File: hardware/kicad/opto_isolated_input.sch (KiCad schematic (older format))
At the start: 9 parts, among them Q1 BC547, Q2 BC337, U6 SFH617A-1, U7 MAX6816

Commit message: Stuff
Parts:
- Q2: value BC337 -> BC337-40
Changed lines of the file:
@@
 AR Path="/62FB890E/62EA87F7" Ref="Q14"  Part="1"
 F 0 "Q2" H 5791 3746 50  0000 L CNN
-F 1 "BC337" H 5791 3655 50  0000 L CNN
+F 1 "BC337-40" H 5791 3655 50  0000 L CNN
 F 2 "Package_TO_SOT_THT:TO-92_Inline" H 5800 3625 50  0001 L CIN
 F 3 "https://diotec.com/tl_files/diotec/files/pdf/datasheets/bc337.pdf" H 5600 3700 50  0001 L CNN
@@
 Text HLabel 7600 3500 2    50   Output ~ 0
 OII_OUT
-Text HLabel 7600 4200 2    50   UnSpc ~ 0
+Text HLabel 7650 4200 2    50   UnSpc ~ 0
 OII_OUT_GND
 $Comp

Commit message: Terak
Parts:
- D10: value IN4148 -> IN4007
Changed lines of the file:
@@
 AR Path="/62FB890E/62FE9B9E" Ref="D16"  Part="1"
 F 0 "D10" H 4750 3250 50  0000 L CNN
-F 1 "IN4148" H 5000 3250 50  0000 L CNN
+F 1 "IN4007" H 5000 3250 50  0000 L CNN
 F 2 "Diode_THT:D_A-405_P2.54mm_Vertical_AnodeUp" H 4950 3300 50  0001 C CNN
 F 3 "~" H 4950 3300 50  0001 C CNN

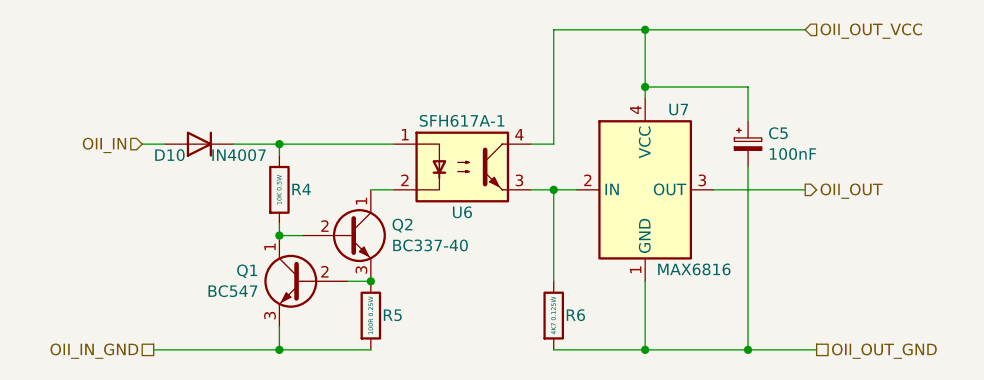
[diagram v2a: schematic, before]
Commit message: Add mount holes
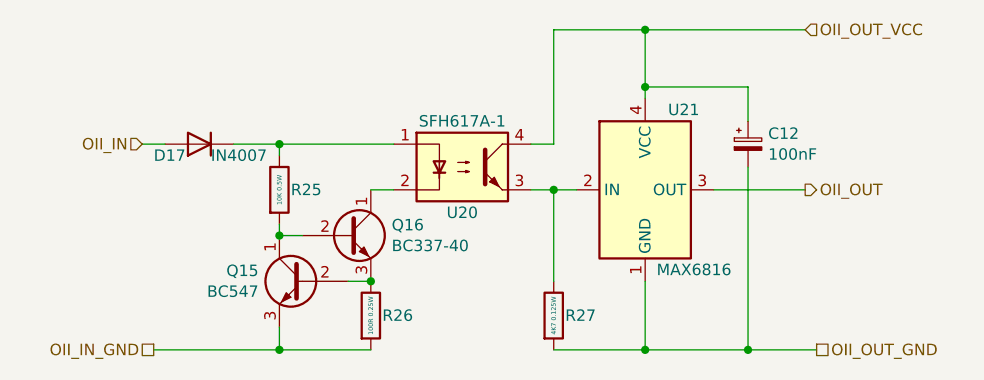
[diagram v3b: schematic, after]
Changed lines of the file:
@@
 AR Path="/62F45EE0/62EBA913" Ref="U16"  Part="1"
 AR Path="/62FB890E/62EBA913" Ref="U18"  Part="1"
-F 0 "U6" H 6100 3200 50  0000 C CNN
+F 0 "U20" H 6100 3200 50  0000 C CNN
 F 1 "SFH617A-1" H 6100 3600 50  0000 C CNN
 F 2 "Package_DIP:DIP-4_W7.62mm" H 5900 3200 50  0001 L CIN
@@
 AR Path="/62F45EE0/62ED7963" Ref="R19"  Part="1"
 AR Path="/62FB890E/62ED7963" Ref="R22"  Part="1"
-F 0 "R4" H 5350 3500 50  0000 L CNN
+F 0 "R25" H 5350 3500 50  0000 L CNN
 F 1 "10K 0.5W" V 5300 3500 20  0000 C CNN
 F 2 "Resistor_THT:R_Axial_DIN0207_L6.3mm_D2.5mm_P2.54mm_Vertical" V 5230 3500 50  0001 C CNN
@@
 AR Path="/62F45EE0/62F493CD" Ref="R20"  Part="1"
 AR Path="/62FB890E/62F493CD" Ref="R23"  Part="1"
-F 0 "R5" H 5750 4050 50  0000 L CNN
+F 0 "R26" H 5750 4050 50  0000 L CNN
 F 1 "100R 0.25W" V 5700 4050 20  0000 C CNN
 F 2 "Resistor_THT:R_Axial_DIN0207_L6.3mm_D2.5mm_P2.54mm_Vertical" V 5630 4050 50  0001 C CNN
@@
 AR Path="/62F45EE0/62EA87F7" Ref="Q12"  Part="1"
 AR Path="/62FB890E/62EA87F7" Ref="Q14"  Part="1"
-F 0 "Q2" H 5791 3746 50  0000 L CNN
+F 0 "Q16" H 5791 3746 50  0000 L CNN
 F 1 "BC337-40" H 5791 3655 50  0000 L CNN
 F 2 "Package_TO_SOT_THT:TO-92_Inline" H 5800 3625 50  0001 L CIN
@@
 AR Path="/62F45EE0/62FE9B9E" Ref="D15"  Part="1"
 AR Path="/62FB890E/62FE9B9E" Ref="D16"  Part="1"
-F 0 "D10" H 4750 3250 50  0000 L CNN
+F 0 "D17" H 4750 3250 50  0000 L CNN
 F 1 "IN4007" H 5000 3250 50  0000 L CNN
 F 2 "Diode_THT:D_A-405_P2.54mm_Vertical_AnodeUp" H 4950 3300 50  0001 C CNN
@@
 AR Path="/62F45EE0/62FB7374" Ref="Q11"  Part="1"
 AR Path="/62FB890E/62FB7374" Ref="Q13"  Part="1"
-F 0 "Q1" H 5591 3946 50  0000 L CNN
+F 0 "Q15" H 5591 3946 50  0000 L CNN
 F 1 "BC547" H 5591 3855 50  0000 L CNN
 F 2 "Package_TO_SOT_THT:TO-92_Inline" H 5600 3825 50  0001 L CIN
@@
 AR Path="/62F45EE0/63451832" Ref="U17"  Part="1"
 AR Path="/62FB890E/63451832" Ref="U19"  Part="1"
-F 0 "U7" H 7000 3850 50  0000 L CNN
+F 0 "U21" H 7000 3850 50  0000 L CNN
 F 1 "MAX6816" H 6950 3150 50  0000 L CNN
 F 2 "Package_TO_SOT_SMD:SOT-143" H 7550 3050 50  0001 C CNN
@@
 AR Path="/62F45EE0/6344909D" Ref="R21"  Part="1"
 AR Path="/62FB890E/6344909D" Ref="R24"  Part="1"
-F 0 "R6" H 6550 4050 50  0000 L CNN
+F 0 "R27" H 6550 4050 50  0000 L CNN
 F 1 "4K7 0.125W" V 6500 4050 20  0000 C CNN
 F 2 "Resistor_SMD:R_0603_1608Metric_Pad0.98x0.95mm_HandSolder" V 6430 4050 50  0001 C CNN
@@
 AR Path="/62FB890E/6344B5F5" Ref="C11"  Part="1"
 AR Path="/63089671/6344B5F5" Ref="C12"  Part="1"
-F 0 "C5" H 7438 3346 50  0000 L CNN
+F 0 "C12" H 7438 3346 50  0000 L CNN
 F 1 "100nF" H 7438 3255 50  0000 L CNN
 F 2 "Capacitor_SMD:CP_Elec_4x4.5" H 7350 3300 50  0001 C CNN

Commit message: Refactor
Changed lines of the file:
@@
 $Descr A4 11693 8268
 encoding utf-8
-Sheet 2 9
+Sheet 4 9
 Title "SIM108 Switch Input Module"
 Date "2022-06-11"
@@
 AR Path="/62F45EE0/62EBA913" Ref="U16"  Part="1"
 AR Path="/62FB890E/62EBA913" Ref="U18"  Part="1"
-F 0 "U20" H 6100 3200 50  0000 C CNN
+F 0 "U10" H 6100 3200 50  0000 C CNN
 F 1 "SFH617A-1" H 6100 3600 50  0000 C CNN
 F 2 "Package_DIP:DIP-4_W7.62mm" H 5900 3200 50  0001 L CIN
@@
 AR Path="/62F45EE0/62ED7963" Ref="R19"  Part="1"
 AR Path="/62FB890E/62ED7963" Ref="R22"  Part="1"
-F 0 "R25" H 5350 3500 50  0000 L CNN
+F 0 "R10" H 5350 3500 50  0000 L CNN
 F 1 "10K 0.5W" V 5300 3500 20  0000 C CNN
 F 2 "Resistor_THT:R_Axial_DIN0207_L6.3mm_D2.5mm_P2.54mm_Vertical" V 5230 3500 50  0001 C CNN
@@
 AR Path="/62F45EE0/62F493CD" Ref="R20"  Part="1"
 AR Path="/62FB890E/62F493CD" Ref="R23"  Part="1"
-F 0 "R26" H 5750 4050 50  0000 L CNN
+F 0 "R11" H 5750 4050 50  0000 L CNN
 F 1 "100R 0.25W" V 5700 4050 20  0000 C CNN
 F 2 "Resistor_THT:R_Axial_DIN0207_L6.3mm_D2.5mm_P2.54mm_Vertical" V 5630 4050 50  0001 C CNN
@@
 AR Path="/62F45EE0/62EA87F7" Ref="Q12"  Part="1"
 AR Path="/62FB890E/62EA87F7" Ref="Q14"  Part="1"
-F 0 "Q16" H 5791 3746 50  0000 L CNN
+F 0 "Q6" H 5791 3746 50  0000 L CNN
 F 1 "BC337-40" H 5791 3655 50  0000 L CNN
 F 2 "Package_TO_SOT_THT:TO-92_Inline" H 5800 3625 50  0001 L CIN
@@
 AR Path="/62F45EE0/62FE9B9E" Ref="D15"  Part="1"
 AR Path="/62FB890E/62FE9B9E" Ref="D16"  Part="1"
-F 0 "D17" H 4750 3250 50  0000 L CNN
+F 0 "D12" H 4750 3250 50  0000 L CNN
 F 1 "IN4007" H 5000 3250 50  0000 L CNN
 F 2 "Diode_THT:D_A-405_P2.54mm_Vertical_AnodeUp" H 4950 3300 50  0001 C CNN
@@
 AR Path="/62F45EE0/62FB7374" Ref="Q11"  Part="1"
 AR Path="/62FB890E/62FB7374" Ref="Q13"  Part="1"
-F 0 "Q15" H 5591 3946 50  0000 L CNN
+F 0 "Q5" H 5591 3946 50  0000 L CNN
 F 1 "BC547" H 5591 3855 50  0000 L CNN
 F 2 "Package_TO_SOT_THT:TO-92_Inline" H 5600 3825 50  0001 L CIN
@@
 AR Path="/62F45EE0/63451832" Ref="U17"  Part="1"
 AR Path="/62FB890E/63451832" Ref="U19"  Part="1"
-F 0 "U21" H 7000 3850 50  0000 L CNN
+F 0 "U11" H 7000 3850 50  0000 L CNN
 F 1 "MAX6816" H 6950 3150 50  0000 L CNN
 F 2 "Package_TO_SOT_SMD:SOT-143" H 7550 3050 50  0001 C CNN
@@
 AR Path="/62F45EE0/6344909D" Ref="R21"  Part="1"
 AR Path="/62FB890E/6344909D" Ref="R24"  Part="1"
-F 0 "R27" H 6550 4050 50  0000 L CNN
+F 0 "R12" H 6550 4050 50  0000 L CNN
 F 1 "4K7 0.125W" V 6500 4050 20  0000 C CNN
 F 2 "Resistor_SMD:R_0603_1608Metric_Pad0.98x0.95mm_HandSolder" V 6430 4050 50  0001 C CNN
@@
 AR Path="/62FB890E/6344B5F5" Ref="C11"  Part="1"
 AR Path="/63089671/6344B5F5" Ref="C12"  Part="1"
-F 0 "C12" H 7438 3346 50  0000 L CNN
+F 0 "C7" H 7438 3346 50  0000 L CNN
 F 1 "100nF" H 7438 3255 50  0000 L CNN
 F 2 "Capacitor_SMD:CP_Elec_4x4.5" H 7350 3300 50  0001 C CNN

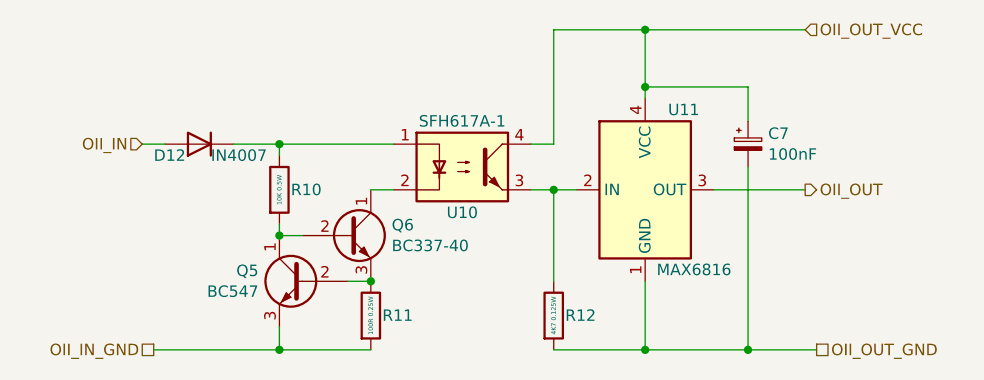
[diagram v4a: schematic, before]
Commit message: Swap passive SMD for TH
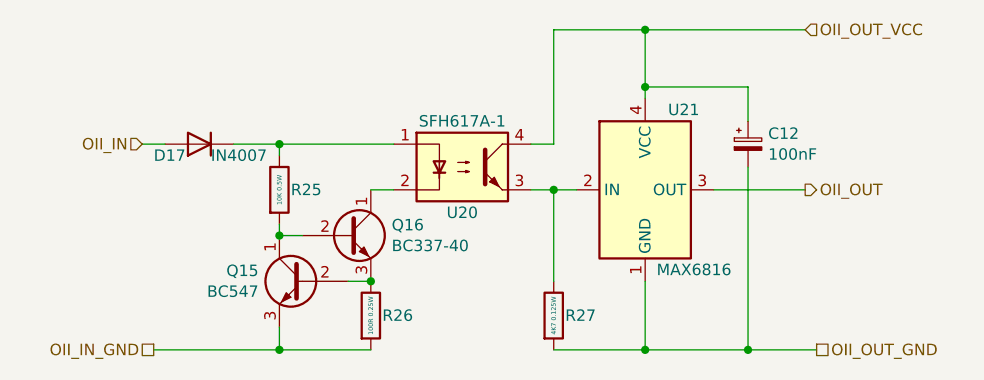
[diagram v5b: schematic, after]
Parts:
- C5: footprint Capacitor_SMD:CP_Elec_4x4.5 -> Capacitor_THT:CP_Radial_D5.0mm_P2.00mm
- R6: footprint Resistor_SMD:R_0603_1608Metric_Pad0.98x0.95mm_HandSolder -> Resistor_THT:R_Axial_DIN0207_L6.3mm_D2.5mm_P2.54mm_Vertical
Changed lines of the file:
@@
 $Descr A4 11693 8268
 encoding utf-8
-Sheet 4 9
+Sheet 9 9
 Title "SIM108 Switch Input Module"
 Date "2022-06-11"
@@
 AR Path="/62F45EE0/62EBA913" Ref="U16"  Part="1"
 AR Path="/62FB890E/62EBA913" Ref="U18"  Part="1"
-F 0 "U10" H 6100 3200 50  0000 C CNN
+F 0 "U20" H 6100 3200 50  0000 C CNN
 F 1 "SFH617A-1" H 6100 3600 50  0000 C CNN
 F 2 "Package_DIP:DIP-4_W7.62mm" H 5900 3200 50  0001 L CIN
@@
 AR Path="/62F45EE0/62ED7963" Ref="R19"  Part="1"
 AR Path="/62FB890E/62ED7963" Ref="R22"  Part="1"
-F 0 "R10" H 5350 3500 50  0000 L CNN
+F 0 "R25" H 5350 3500 50  0000 L CNN
 F 1 "10K 0.5W" V 5300 3500 20  0000 C CNN
 F 2 "Resistor_THT:R_Axial_DIN0207_L6.3mm_D2.5mm_P2.54mm_Vertical" V 5230 3500 50  0001 C CNN
@@
 AR Path="/62F45EE0/62F493CD" Ref="R20"  Part="1"
 AR Path="/62FB890E/62F493CD" Ref="R23"  Part="1"
-F 0 "R11" H 5750 4050 50  0000 L CNN
+F 0 "R26" H 5750 4050 50  0000 L CNN
 F 1 "100R 0.25W" V 5700 4050 20  0000 C CNN
 F 2 "Resistor_THT:R_Axial_DIN0207_L6.3mm_D2.5mm_P2.54mm_Vertical" V 5630 4050 50  0001 C CNN
@@
 AR Path="/62F45EE0/62EA87F7" Ref="Q12"  Part="1"
 AR Path="/62FB890E/62EA87F7" Ref="Q14"  Part="1"
-F 0 "Q6" H 5791 3746 50  0000 L CNN
+F 0 "Q16" H 5791 3746 50  0000 L CNN
 F 1 "BC337-40" H 5791 3655 50  0000 L CNN
 F 2 "Package_TO_SOT_THT:TO-92_Inline" H 5800 3625 50  0001 L CIN
@@
 AR Path="/62F45EE0/62FE9B9E" Ref="D15"  Part="1"
 AR Path="/62FB890E/62FE9B9E" Ref="D16"  Part="1"
-F 0 "D12" H 4750 3250 50  0000 L CNN
+F 0 "D17" H 4750 3250 50  0000 L CNN
 F 1 "IN4007" H 5000 3250 50  0000 L CNN
 F 2 "Diode_THT:D_A-405_P2.54mm_Vertical_AnodeUp" H 4950 3300 50  0001 C CNN
@@
 AR Path="/62F45EE0/62FB7374" Ref="Q11"  Part="1"
 AR Path="/62FB890E/62FB7374" Ref="Q13"  Part="1"
-F 0 "Q5" H 5591 3946 50  0000 L CNN
+F 0 "Q15" H 5591 3946 50  0000 L CNN
 F 1 "BC547" H 5591 3855 50  0000 L CNN
 F 2 "Package_TO_SOT_THT:TO-92_Inline" H 5600 3825 50  0001 L CIN
@@
 AR Path="/62F45EE0/63451832" Ref="U17"  Part="1"
 AR Path="/62FB890E/63451832" Ref="U19"  Part="1"
-F 0 "U11" H 7000 3850 50  0000 L CNN
+F 0 "U21" H 7000 3850 50  0000 L CNN
 F 1 "MAX6816" H 6950 3150 50  0000 L CNN
 F 2 "Package_TO_SOT_SMD:SOT-143" H 7550 3050 50  0001 C CNN
@@
 AR Path="/62F45EE0/6344909D" Ref="R21"  Part="1"
 AR Path="/62FB890E/6344909D" Ref="R24"  Part="1"
-F 0 "R12" H 6550 4050 50  0000 L CNN
+F 0 "R27" H 6550 4050 50  0000 L CNN
 F 1 "4K7 0.125W" V 6500 4050 20  0000 C CNN
-F 2 "Resistor_SMD:R_0603_1608Metric_Pad0.98x0.95mm_HandSolder" V 6430 4050 50  0001 C CNN
+F 2 "Resistor_THT:R_Axial_DIN0207_L6.3mm_D2.5mm_P2.54mm_Vertical" V 6430 4050 50  0001 C CNN
 F 3 "~" H 6500 4050 50  0001 C CNN
 F 4 "0.125W" V 6600 4050 50  0001 C CNN "Power"
@@
 AR Path="/62FB890E/6344B5F5" Ref="C11"  Part="1"
 AR Path="/63089671/6344B5F5" Ref="C12"  Part="1"
-F 0 "C7" H 7438 3346 50  0000 L CNN
+F 0 "C12" H 7438 3346 50  0000 L CNN
 F 1 "100nF" H 7438 3255 50  0000 L CNN
-F 2 "Capacitor_SMD:CP_Elec_4x4.5" H 7350 3300 50  0001 C CNN
+F 2 "Capacitor_THT:CP_Radial_D5.0mm_P2.00mm" H 7350 3300 50  0001 C CNN
 F 3 "~" H 7350 3300 50  0001 C CNN
 	1    7350 3300

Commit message: Migrate to Teens 4.0
3.3V inputs
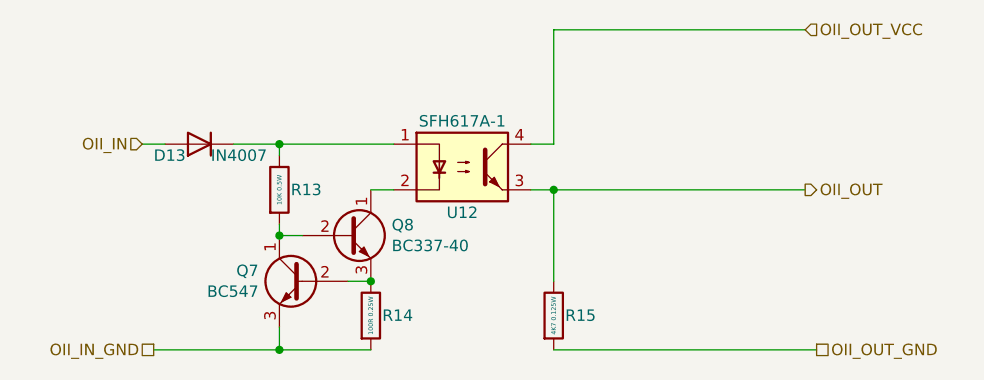
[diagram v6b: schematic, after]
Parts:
- removed C5: 100nF, Capacitor_THT:CP_Radial_D5.0mm_P2.00mm, symbol Device:CP_Small
- removed U7: MAX6816, Package_TO_SOT_SMD:SOT-143, symbol Interface:MAX6816
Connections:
- net OII_OUT: now also R6.1, U6.3
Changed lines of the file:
@@
 $Descr A4 11693 8268
 encoding utf-8
-Sheet 9 9
+Sheet 5 9
 Title "SIM108 Switch Input Module"
 Date "2022-06-11"
@@
 AR Path="/62F45EE0/62EBA913" Ref="U16"  Part="1"
 AR Path="/62FB890E/62EBA913" Ref="U18"  Part="1"
-F 0 "U20" H 6100 3200 50  0000 C CNN
+F 0 "U12" H 6100 3200 50  0000 C CNN
 F 1 "SFH617A-1" H 6100 3600 50  0000 C CNN
 F 2 "Package_DIP:DIP-4_W7.62mm" H 5900 3200 50  0001 L CIN
@@
 AR Path="/62F45EE0/62ED7963" Ref="R19"  Part="1"
 AR Path="/62FB890E/62ED7963" Ref="R22"  Part="1"
-F 0 "R25" H 5350 3500 50  0000 L CNN
+F 0 "R13" H 5350 3500 50  0000 L CNN
 F 1 "10K 0.5W" V 5300 3500 20  0000 C CNN
 F 2 "Resistor_THT:R_Axial_DIN0207_L6.3mm_D2.5mm_P2.54mm_Vertical" V 5230 3500 50  0001 C CNN
@@
 AR Path="/62F45EE0/62F493CD" Ref="R20"  Part="1"
 AR Path="/62FB890E/62F493CD" Ref="R23"  Part="1"
-F 0 "R26" H 5750 4050 50  0000 L CNN
+F 0 "R14" H 5750 4050 50  0000 L CNN
 F 1 "100R 0.25W" V 5700 4050 20  0000 C CNN
 F 2 "Resistor_THT:R_Axial_DIN0207_L6.3mm_D2.5mm_P2.54mm_Vertical" V 5630 4050 50  0001 C CNN
@@
 AR Path="/62F45EE0/62EA87F7" Ref="Q12"  Part="1"
 AR Path="/62FB890E/62EA87F7" Ref="Q14"  Part="1"
-F 0 "Q16" H 5791 3746 50  0000 L CNN
+F 0 "Q8" H 5791 3746 50  0000 L CNN
 F 1 "BC337-40" H 5791 3655 50  0000 L CNN
 F 2 "Package_TO_SOT_THT:TO-92_Inline" H 5800 3625 50  0001 L CIN
@@
 AR Path="/62F45EE0/62FE9B9E" Ref="D15"  Part="1"
 AR Path="/62FB890E/62FE9B9E" Ref="D16"  Part="1"
-F 0 "D17" H 4750 3250 50  0000 L CNN
+F 0 "D13" H 4750 3250 50  0000 L CNN
 F 1 "IN4007" H 5000 3250 50  0000 L CNN
 F 2 "Diode_THT:D_A-405_P2.54mm_Vertical_AnodeUp" H 4950 3300 50  0001 C CNN
@@
 AR Path="/62F45EE0/62FB7374" Ref="Q11"  Part="1"
 AR Path="/62FB890E/62FB7374" Ref="Q13"  Part="1"
-F 0 "Q15" H 5591 3946 50  0000 L CNN
+F 0 "Q7" H 5591 3946 50  0000 L CNN
 F 1 "BC547" H 5591 3855 50  0000 L CNN
 F 2 "Package_TO_SOT_THT:TO-92_Inline" H 5600 3825 50  0001 L CIN
@@
 Text HLabel 7650 4200 2    50   UnSpc ~ 0
 OII_OUT_GND
-$Comp
-L Interface:MAX6816 U7
-U 1 1 63451832
-P 6900 3500
-AR Path="/62FB7846/63451832" Ref="U7"  Part="1"
-AR Path="/63089671/63451832" Ref="U21"  Part="1"
-AR Path="/63103CAF/63451832" Ref="U9"  Part="1"
-AR Path="/62F64647/63451832" Ref="U11"  Part="1"
-AR Path="/62FD589D/63451832" Ref="U13"  Part="1"
-AR Path="/63041ECA/63451832" Ref="U15"  Part="1"
-AR Path="/62F45EE0/63451832" Ref="U17"  Part="1"
-AR Path="/62FB890E/63451832" Ref="U19"  Part="1"
-F 0 "U21" H 7000 3850 50  0000 L CNN
-F 1 "MAX6816" H 6950 3150 50  0000 L CNN
-F 2 "Package_TO_SOT_SMD:SOT-143" H 7550 3050 50  0001 C CNN
-F 3 "https://datasheets.maximintegrated.com/en/ds/1896.pdf" H 6900 3500 50  0001 C CNN
-	1    6900 3500
-	1    0    0    -1
-$EndComp
-Wire Wire Line
-	7200 3500 7600 3500
 Text HLabel 7600 2800 2    50   Input ~ 0
 OII_OUT_VCC
 Wire Wire Line
-	6900 3900 6900 4200
-Wire Wire Line
-	6900 4200 7350 4200
-Wire Wire Line
-	6900 3100 6900 3050
-Wire Wire Line
-	6900 2800 7600 2800
-Wire Wire Line
 	6400 3500 6500 3500
 Wire Wire Line
@@
 Wire Wire Line
 	6500 3300 6500 2800
-Wire Wire Line
-	6500 2800 6900 2800
-Connection ~ 6900 2800
 $Comp
 L Device:R R6
@@
 AR Path="/62F45EE0/6344909D" Ref="R21"  Part="1"
 AR Path="/62FB890E/6344909D" Ref="R24"  Part="1"
-F 0 "R27" H 6550 4050 50  0000 L CNN
+F 0 "R15" H 6550 4050 50  0000 L CNN
 F 1 "4K7 0.125W" V 6500 4050 20  0000 C CNN
 F 2 "Resistor_THT:R_Axial_DIN0207_L6.3mm_D2.5mm_P2.54mm_Vertical" V 6430 4050 50  0001 C CNN
@@
 $EndComp
 Wire Wire Line
-	6900 4200 6500 4200
-Connection ~ 6900 4200
-Wire Wire Line
 	6500 3900 6500 3500
 Connection ~ 6500 3500
 Wire Wire Line
-	6500 3500 6600 3500
-$Comp
-L Device:CP_Small C5
-U 1 1 6344B5F5
-P 7350 3300
-AR Path="/62FB7846/6344B5F5" Ref="C5"  Part="1"
-AR Path="/63103CAF/6344B5F5" Ref="C6"  Part="1"
-AR Path="/62F64647/6344B5F5" Ref="C7"  Part="1"
-AR Path="/62FD589D/6344B5F5" Ref="C8"  Part="1"
-AR Path="/63041ECA/6344B5F5" Ref="C9"  Part="1"
-AR Path="/62F45EE0/6344B5F5" Ref="C10"  Part="1"
-AR Path="/62FB890E/6344B5F5" Ref="C11"  Part="1"
-AR Path="/63089671/6344B5F5" Ref="C12"  Part="1"
-F 0 "C12" H 7438 3346 50  0000 L CNN
-F 1 "100nF" H 7438 3255 50  0000 L CNN
-F 2 "Capacitor_THT:CP_Radial_D5.0mm_P2.00mm" H 7350 3300 50  0001 C CNN
-F 3 "~" H 7350 3300 50  0001 C CNN
-	1    7350 3300
-	1    0    0    -1
-$EndComp
-Wire Wire Line
-	7350 3200 7350 3050
-Wire Wire Line
-	7350 3050 6900 3050
-Connection ~ 6900 3050
-Wire Wire Line
-	6900 3050 6900 2800
-Wire Wire Line
-	7350 3400 7350 4200
-Connection ~ 7350 4200
-Wire Wire Line
-	7350 4200 7650 4200
-Wire Wire Line
 	4750 4200 5300 4200
 Wire Wire Line
 	4800 3300 4700 3300
+Wire Wire Line
+	6500 2800 7600 2800
+Wire Wire Line
+	6500 4200 7650 4200
+Wire Wire Line
+	6500 3500 7600 3500
 $EndSCHEMATC

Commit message: Tweaks
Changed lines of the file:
@@
 AR Path="/62F45EE0/62EBA913" Ref="U16"  Part="1"
 AR Path="/62FB890E/62EBA913" Ref="U18"  Part="1"
-F 0 "U12" H 6100 3200 50  0000 C CNN
+F 0 "U20" H 6100 3200 50  0000 C CNN
 F 1 "SFH617A-1" H 6100 3600 50  0000 C CNN
 F 2 "Package_DIP:DIP-4_W7.62mm" H 5900 3200 50  0001 L CIN
@@
 AR Path="/62F45EE0/62ED7963" Ref="R19"  Part="1"
 AR Path="/62FB890E/62ED7963" Ref="R22"  Part="1"
-F 0 "R13" H 5350 3500 50  0000 L CNN
+F 0 "R25" H 5350 3500 50  0000 L CNN
 F 1 "10K 0.5W" V 5300 3500 20  0000 C CNN
 F 2 "Resistor_THT:R_Axial_DIN0207_L6.3mm_D2.5mm_P2.54mm_Vertical" V 5230 3500 50  0001 C CNN
@@
 AR Path="/62F45EE0/62F493CD" Ref="R20"  Part="1"
 AR Path="/62FB890E/62F493CD" Ref="R23"  Part="1"
-F 0 "R14" H 5750 4050 50  0000 L CNN
+F 0 "R26" H 5750 4050 50  0000 L CNN
 F 1 "100R 0.25W" V 5700 4050 20  0000 C CNN
 F 2 "Resistor_THT:R_Axial_DIN0207_L6.3mm_D2.5mm_P2.54mm_Vertical" V 5630 4050 50  0001 C CNN
@@
 AR Path="/62F45EE0/62EA87F7" Ref="Q12"  Part="1"
 AR Path="/62FB890E/62EA87F7" Ref="Q14"  Part="1"
-F 0 "Q8" H 5791 3746 50  0000 L CNN
+F 0 "Q16" H 5791 3746 50  0000 L CNN
 F 1 "BC337-40" H 5791 3655 50  0000 L CNN
 F 2 "Package_TO_SOT_THT:TO-92_Inline" H 5800 3625 50  0001 L CIN
@@
 AR Path="/62F45EE0/62FE9B9E" Ref="D15"  Part="1"
 AR Path="/62FB890E/62FE9B9E" Ref="D16"  Part="1"
-F 0 "D13" H 4750 3250 50  0000 L CNN
+F 0 "D17" H 4750 3250 50  0000 L CNN
 F 1 "IN4007" H 5000 3250 50  0000 L CNN
 F 2 "Diode_THT:D_A-405_P2.54mm_Vertical_AnodeUp" H 4950 3300 50  0001 C CNN
@@
 AR Path="/62F45EE0/62FB7374" Ref="Q11"  Part="1"
 AR Path="/62FB890E/62FB7374" Ref="Q13"  Part="1"
-F 0 "Q7" H 5591 3946 50  0000 L CNN
+F 0 "Q15" H 5591 3946 50  0000 L CNN
 F 1 "BC547" H 5591 3855 50  0000 L CNN
 F 2 "Package_TO_SOT_THT:TO-92_Inline" H 5600 3825 50  0001 L CIN
@@
 AR Path="/62F45EE0/6344909D" Ref="R21"  Part="1"
 AR Path="/62FB890E/6344909D" Ref="R24"  Part="1"
-F 0 "R15" H 6550 4050 50  0000 L CNN
+F 0 "R27" H 6550 4050 50  0000 L CNN
 F 1 "4K7 0.125W" V 6500 4050 20  0000 C CNN
 F 2 "Resistor_THT:R_Axial_DIN0207_L6.3mm_D2.5mm_P2.54mm_Vertical" V 6430 4050 50  0001 C CNN
